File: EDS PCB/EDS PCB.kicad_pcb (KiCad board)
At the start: 2 copper layers, 100 x 100 mm, 1 part

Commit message: EDS New shit
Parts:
- removed the REF** at (144.0, 41.0)
- added ?: , , F.Cu at (83.0, 84.0)
- added ?: , , F.Cu at (83.0, 69.0)
- added ?: , , F.Cu at (83.0, 99.0)
- added REF**: EDS_Input_Connector, EDS_Project_Library:EDS_Input_Connector, F.Cu at (47.0, 99.0)
- added REF**: R2, Resistor_THT:R_Axial_DIN0207_L6.3mm_D2.5mm_P15.24mm_Horizontal, F.Cu at (57.0, 84.0)
- added REF**: R3, Resistor_THT:R_Axial_DIN0207_L6.3mm_D2.5mm_P15.24mm_Horizontal, F.Cu at (57.0, 69.0)
- added REF**: R1, Resistor_THT:R_Axial_DIN0207_L6.3mm_D2.5mm_P15.24mm_Horizontal, F.Cu at (57.4, 99.0)
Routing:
- net (no net): track 0.00 -> 62.3 mm
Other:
- board size 100 x 100 mm -> 96 x 100 mm
- board text added: "P1"
- board text added: "P2"
- board text added: "P3"

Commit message: EDS Electrodes
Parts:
- added ?: , clipboard:bf32c9e1-eea9-421a-b75f-750c3fb07239, F.Cu at (47.0, 54.5)
- added REF**: MountingHole_3.2mm_M3, MountingHole:MountingHole_3.2mm_M3, F.Cu at (203.0, 125.0)
- added REF**: MountingHole_3.2mm_M3, MountingHole:MountingHole_3.2mm_M3, F.Cu at (202.5, 34.5)
- added REF**: MountingHole_3.2mm_M3, MountingHole:MountingHole_3.2mm_M3, F.Cu at (42.5, 125.5)
- added REF**: MountingHole_3.2mm_M3, MountingHole:MountingHole_3.2mm_M3, F.Cu at (42.5, 34.5)
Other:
- board size 96 x 100 mm -> 169.5 x 111.5 mm
- board text added: "WARNING! 1kV!"

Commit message: EDS Electrode Array
This sucks
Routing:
- added copper zone on F.Cu, net (none)
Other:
- board text added: "MountingHole_3.2mm_M3"

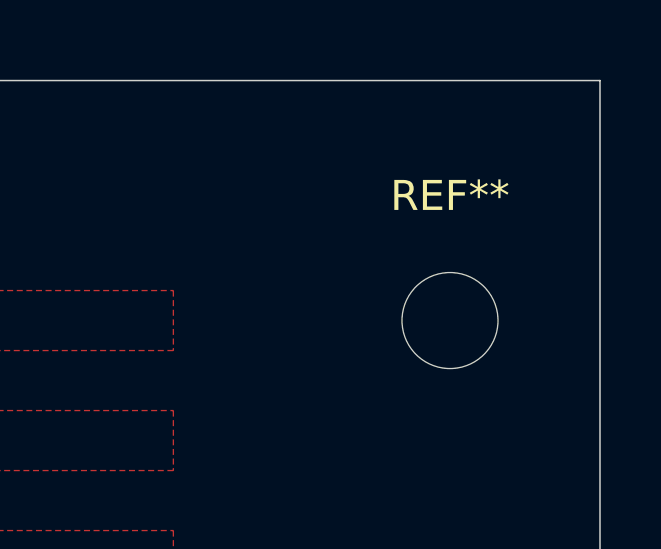
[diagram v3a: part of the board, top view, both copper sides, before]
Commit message: EDS Phase Nets Updated
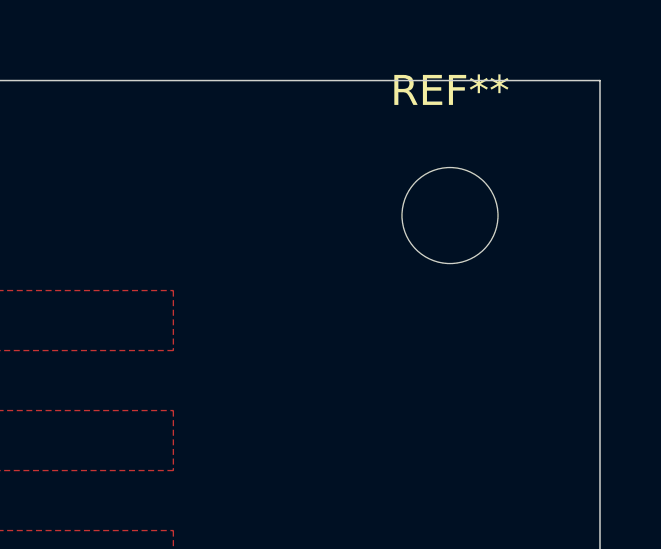
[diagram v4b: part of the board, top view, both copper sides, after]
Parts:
- moved REF** 3.50 mm to (202.5, 31.0)
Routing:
- added copper zone on F.Cu, net Phase1
- added copper zone on F.Cu, net Phase2
- added copper zone on F.Cu, net Phase3
- removed copper zone on F.Cu, net (none)
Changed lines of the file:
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@@
 	)
 	(net 0 "")
+	(net 1 "Phase1")
+	(net 2 "Phase2")
+	(net 3 "Phase3")
 	(footprint "clipboard:bf32c9e1-eea9-421a-b75f-750c3fb07239"
 		(layer "F.Cu")
@@
 	(footprint "MountingHole:MountingHole_3.2mm_M3"
 		(layer "F.Cu")
-		(at 202.5 34.5)
+		(at 202.5 31)
 		(descr "Mounting Hole 3.2mm, M3, no annular, generated by kicad-footprint-generator mountinghole.py")
 		(tags "mountinghole M3")
@@
 	)
 	(zone
-		(net 0)
-		(net_name "")
+		(net 2)
+		(net_name "Phase2")
 		(layer "F.Cu")
 		(name "Phase1")
@@
 		(min_thickness 0.5)
 		(filled_areas_thickness no)
-		(fill
+		(fill yes
 			(thermal_gap 0.5)
 			(thermal_bridge_width 0.5)
@@
 	)
 	(zone
-		(net 0)
-		(net_name "")
+		(net 3)
+		(net_name "Phase3")
 		(layer "F.Cu")
 		(name "Phase1")
@@
 		(min_thickness 0.5)
 		(filled_areas_thickness no)
-		(fill
+		(fill yes
 			(thermal_gap 0.5)
 			(thermal_bridge_width 0.5)
@@
 	)
 	(zone
-		(net 0)
-		(net_name "")
+		(net 3)
+		(net_name "Phase3")
 		(layer "F.Cu")
 		(name "Phase1")
@@
 		(min_thickness 0.5)
 		(filled_areas_thickness no)
-		(fill
+		(fill yes
 			(thermal_gap 0.5)
 			(thermal_bridge_width 0.5)
@@
 	)
 	(zone
-		(net 0)
-		(net_name "")
+		(net 3)
+		(net_name "Phase3")
 		(layer "F.Cu")
 		(name "Phase1")
@@
 		(min_thickness 0.5)
 		(filled_areas_thickness no)
-		(fill
+		(fill yes
 			(thermal_gap 0.5)
 			(thermal_bridge_width 0.5)
@@
 	)
 	(zone
-		(net 0)
-		(net_name "")
+		(net 3)
+		(net_name "Phase3")
 		(layer "F.Cu")
 		(name "Phase1")
@@
 		(min_thickness 0.5)
 		(filled_areas_thickness no)
-		(fill
+		(fill yes
 			(thermal_gap 0.5)
 			(thermal_bridge_width 0.5)
@@
 	)
 	(zone
-		(net 0)
-		(net_name "")
+		(net 1)
+		(net_name "Phase1")
 		(layer "F.Cu")
 		(name "Phase1")
@@
 		(min_thickness 0.5)
 		(filled_areas_thickness no)
-		(fill
+		(fill yes
 			(thermal_gap 0.5)
 			(thermal_bridge_width 0.5)
@@
 	)
 	(zone
-		(net 0)
-		(net_name "")
+		(net 2)
+		(net_name "Phase2")
 		(layer "F.Cu")
 		(name "Phase1")
@@
 		(min_thickness 0.5)
 		(filled_areas_thickness no)
-		(fill
+		(fill yes
 			(thermal_gap 0.5)
 			(thermal_bridge_width 0.5)
@@
 	)
 	(zone
-		(net 0)
-		(net_name "")
+		(net 1)
+		(net_name "Phase1")
 		(layer "F.Cu")
 		(name "Phase1")
@@
 		(min_thickness 0.5)
 		(filled_areas_thickness no)
-		(fill
+		(fill yes
 			(thermal_gap 0.5)
 			(thermal_bridge_width 0.5)
@@
 	)
 	(zone
-		(net 0)
-		(net_name "")
+		(net 1)
+		(net_name "Phase1")
 		(layer "F.Cu")
 		(name "Phase1")
@@
 		(min_thickness 0.5)
 		(filled_areas_thickness no)
-		(fill
+		(fill yes
 			(thermal_gap 0.5)
 			(thermal_bridge_width 0.5)
@@
 	)
 	(zone
-		(net 0)
-		(net_name "")
+		(net 1)
+		(net_name "Phase1")
 		(layer "F.Cu")
 		(name "Phase1")
@@
 		(min_thickness 0.5)
 		(filled_areas_thickness no)
-		(fill
+		(fill yes
 			(thermal_gap 0.5)
 			(thermal_bridge_width 0.5)
@@
 	)
 	(zone
-		(net 0)
-		(net_name "")
+		(net 3)
+		(net_name "Phase3")
 		(layer "F.Cu")
 		(name "Phase1")
@@
 		(min_thickness 0.5)
 		(filled_areas_thickness no)
-		(fill
+		(fill yes
 			(thermal_gap 0.5)
 			(thermal_bridge_width 0.5)
@@
 	)
 	(zone
-		(net 0)
-		(net_name "")
+		(net 2)
+		(net_name "Phase2")
 		(layer "F.Cu")
 		(name "Phase1")
@@
 		(min_thickness 0.5)
 		(filled_areas_thickness no)
-		(fill
+		(fill yes
 			(thermal_gap 0.5)
 			(thermal_bridge_width 0.5)
@@
 	)
 	(zone
-		(net 0)
-		(net_name "")
+		(net 2)
+		(net_name "Phase2")
 		(layer "F.Cu")
 		(name "Phase1")
@@
 		(min_thickness 0.5)
 		(filled_areas_thickness no)
-		(fill
+		(fill yes
 			(thermal_gap 0.5)
 			(thermal_bridge_width 0.5)
@@
 	)
 	(zone
-		(net 0)
-		(net_name "")
+		(net 1)
+		(net_name "Phase1")
 		(layer "F.Cu")
 		(name "Phase1")
@@
 		(min_thickness 0.5)
 		(filled_areas_thickness no)
-		(fill
+		(fill yes
 			(thermal_gap 0.5)
 			(thermal_bridge_width 0.5)
@@
 	)
 	(zone
-		(net 0)
-		(net_name "")
+		(net 3)
+		(net_name "Phase3")
 		(layer "F.Cu")
 		(name "Phase1")
@@
 		(min_thickness 0.5)
 		(filled_areas_thickness no)
-		(fill
+		(fill yes
 			(thermal_gap 0.5)
 			(thermal_bridge_width 0.5)
@@
 	)
 	(zone
-		(net 0)
-		(net_name "")
+		(net 2)
+		(net_name "Phase2")
 		(layer "F.Cu")
 		(name "Phase1")
@@
 		(min_thickness 0.5)
 		(filled_areas_thickness no)
-		(fill
+		(fill yes
 			(thermal_gap 0.5)
 			(thermal_bridge_width 0.5)
@@
 	)
 	(zone
-		(net 0)
-		(net_name "")
+		(net 1)
+		(net_name "Phase1")
 		(layer "F.Cu")
 		(name "Phase1")
@@
 		(min_thickness 0.5)
 		(filled_areas_thickness no)
-		(fill
+		(fill yes
 			(thermal_gap 0.5)
 			(thermal_bridge_width 0.5)
@@
 	)
 	(zone
-		(net 0)
-		(net_name "")
+		(net 2)
+		(net_name "Phase2")
 		(layer "F.Cu")
 		(name "Phase1")
@@
 		(min_thickness 0.5)
 		(filled_areas_thickness no)
-		(fill
+		(fill yes
 			(thermal_gap 0.5)
 			(thermal_bridge_width 0.5)
@@
 	)
 	(zone
-		(net 0)
-		(net_name "")
+		(net 1)
+		(net_name "Phase1")
 		(layer "F.Cu")
 		(name "Phase1")
@@
 		(min_thickness 0.5)
 		(filled_areas_thickness no)
-		(fill
+		(fill yes
 			(thermal_gap 0.5)
 			(thermal_bridge_width 0.5)
@@
 	)
 	(zone
-		(net 0)
-		(net_name "")
+		(net 1)
+		(net_name "Phase1")
 		(layer "F.Cu")
 		(name "Phase1")
@@
 		(min_thickness 0.5)
 		(filled_areas_thickness no)
-		(fill
+		(fill yes
 			(thermal_gap 0.5)
 			(thermal_bridge_width 0.5)
@@
 	)
 	(zone
-		(net 0)
-		(net_name "")
+		(net 2)
+		(net_name "Phase2")
 		(layer "F.Cu")
 		(name "Phase1")
@@
 		(min_thickness 0.5)
 		(filled_areas_thickness no)
-		(fill
+		(fill yes
 			(thermal_gap 0.5)
 			(thermal_bridge_width 0.5)
@@
 	)
 	(zone
-		(net 0)
-		(net_name "")
+		(net 2)
+		(net_name "Phase2")
 		(layer "F.Cu")
 		(name "Phase1")
@@
 		(min_thickness 0.5)
 		(filled_areas_thickness no)
-		(fill
+		(fill yes
 			(thermal_gap 0.5)
 			(thermal_bridge_width 0.5)
@@
 	)
 	(zone
-		(net 0)
-		(net_name "")
+		(net 3)
+		(net_name "Phase3")
 		(layer "F.Cu")
 		(name "Phase1")
@@
 		(min_thickness 0.5)
 		(filled_areas_thickness no)
-		(fill
+		(fill yes
 			(thermal_gap 0.5)
 			(thermal_bridge_width 0.5)
@@
 	)
 	(zone
-		(net 0)
-		(net_name "")
+		(net 3)
+		(net_name "Phase3")
 		(layer "F.Cu")
 		(name "Phase1")
@@
 		(min_thickness 0.5)
 		(filled_areas_thickness no)
-		(fill
+		(fill yes
 			(thermal_gap 0.5)
 			(thermal_bridge_width 0.5)

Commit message: Tried Finishing it, but nahhhh
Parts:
- removed the ? at (83.0, 84.0)
- removed the ? at (83.0, 69.0)
- removed the ? at (83.0, 99.0)
- added REF**: EDS_Input_Connector, EDS_Project_Library:EDS_Input_Connector, F.Cu at (70.8, 110.0)
- moved REF** 60.7 mm to (260.5, 144.5)
- moved REF** 56.1 mm to (258.5, 28.0)
- moved REF** 22.9 mm to (29.8, 144.5)
- moved ? 16.8 mm to (34.2, 65.5)
- moved REF** 16.8 mm to (34.2, 110.0)
- moved REF** 16.8 mm to (44.2, 95.0)
- moved REF** 16.8 mm to (44.2, 80.0)
- moved REF** 16.8 mm to (44.6, 110.0)
- moved REF** 15.1 mm to (30.0, 26.0)
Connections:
- REF** pad 2: (no net) -> Phase2
- REF** pad 2: (no net) -> Phase3
- REF** pad 2: (no net) -> Phase1
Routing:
- net Phase2: track 0.00 -> 1262.9 mm
- net Phase1: track 0.00 -> 965.2 mm
- net Phase3: track 0.00 -> 759.3 mm
- net (no net): track 62.3 -> 30.4 mm
- removed copper zone on F.Cu, net Phase1
- removed copper zone on F.Cu, net Phase2
- removed copper zone on F.Cu, net Phase3
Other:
- board size 169.5 x 111.5 mm -> 240 x 127.5 mm
- board text removed: "MountingHole_3.2mm_M3"
